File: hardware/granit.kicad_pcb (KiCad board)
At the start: 4 copper layers, 92 x 100 mm, 118 parts, among them IC1 ASM1061, J1 12V Barrel, J2 12V Screw Terminal, J3 RJ45_RB1-125B8G1A, J6 PCM12SMTR, J7 USB_C_Receptacle_USB2.0_14P, J8 BM03B-SRSS-TB, J9 SATA_22pin, Q1 FDS4435BZ, Q2 FDS4435BZ, Q3 FDS4435BZ, Q4 2N7002, Q5 2N7002, Q6 2N7002, SW1 SW_Push, U1 NCP1117-3.3_SOT223, U2 AP64501SP-13, U3 74AHCT1G125, U4 DS3231MZ, U5 USBLC6-2SC6, U6 74AHCT1G32, Y1 25MHz

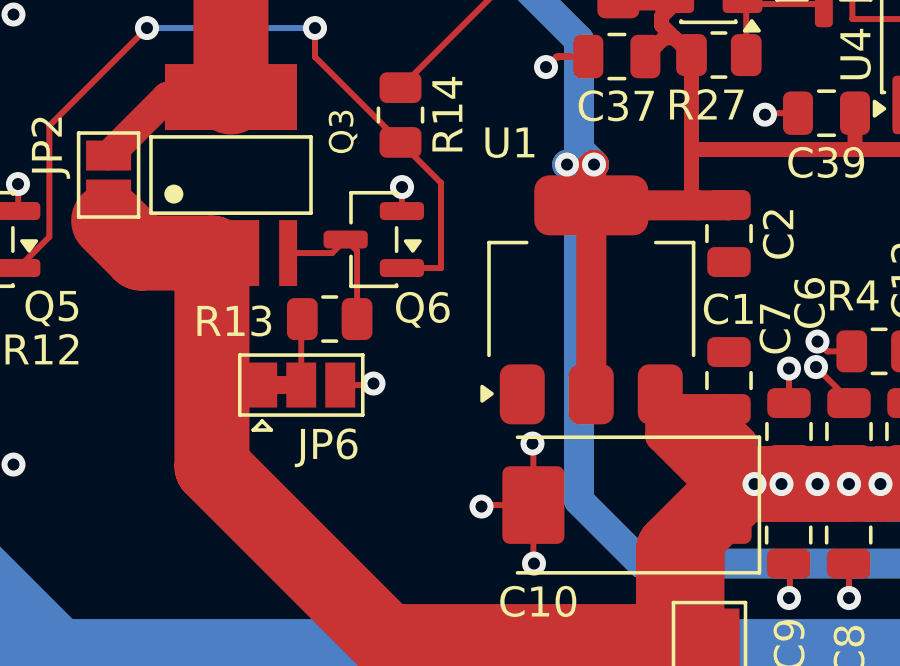
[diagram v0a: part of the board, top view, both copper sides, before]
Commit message: feat: add R15 (100K) pull-down on SATA N-FET gate for boot safety
Ensures SATA power stays OFF during boot before GPIO5 is configured.
R15 pulls Net-(Q5-G) to GND. Normal operation unaffected (3.0V at gate
with GPIO5 high, well above 2N7002 threshold).
DRC: 0 errors, 1 cosmetic warning (Y1 silkscreen).
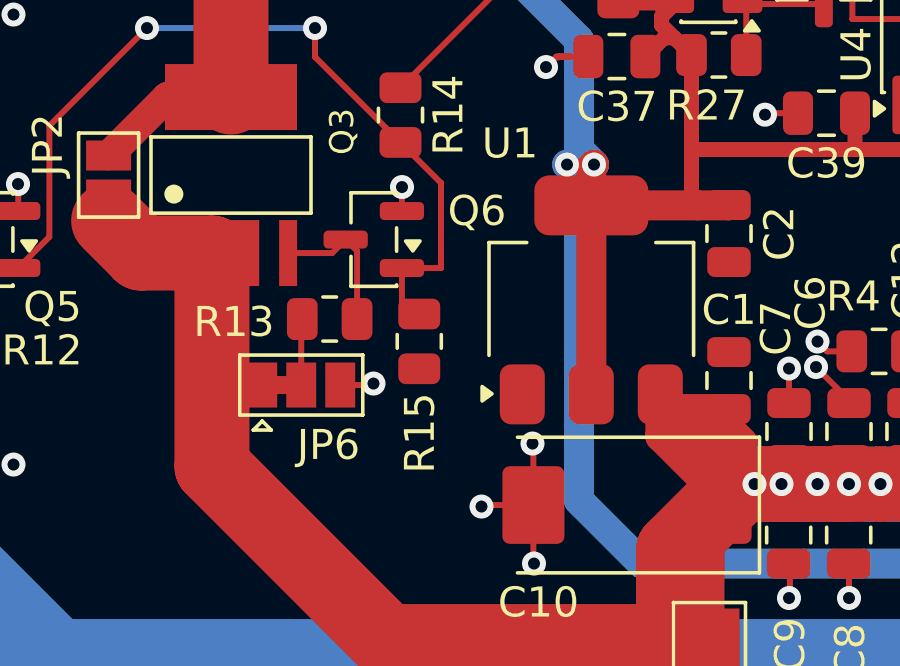
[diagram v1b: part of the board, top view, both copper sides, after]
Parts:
- added R15: 100K, Resistor_SMD:R_0805_2012Metric, F.Cu at (50.0, 107.3)
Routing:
- net Net-(Q5-G): track 26.4 -> 28.3 mm
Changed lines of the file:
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@@
 		(tags "SOT TO_SOT_SMD")
 		(property "Reference" "Q6"
-			(at -1.639999 -2.3 0)
+			(at -3.439999 0.95 0)
 			(layer "F.SilkS")
 			(effects
@@
 		)
 	)
+	(footprint "Resistor_SMD:R_0805_2012Metric"
+		(layer "F.Cu")
+		(at 49.975 107.345 90)
+		(descr "Resistor SMD 0805 (2012 Metric), square (rectangular) end terminal, IPC-7351 nominal, (Body size source: IPC-SM-782 page 72, https://www.pcb-3d.com/wordpress/wp-content/uploads/ipc-sm-782a_amendment_1_and_2.pdf)")
+		(tags "resistor")
+		(property "Reference" "R15"
+			(at -3.055 0.025 90)
+			(layer "F.SilkS")
+			(effects
+				(font
+					(size 1 1)
+					(thickness 0.15)
+				)
+			)
+		)
+		(property "Value" "100K"
+			(at 0 1.65 90)
+			(layer "F.Fab")
+			(effects
+				(font
+					(size 1 1)
+					(thickness 0.15)
+				)
+			)
+		)
+		(property "Datasheet" ""
+			(at 0 0 90)
+			(layer "F.Fab")
+			(hide yes)
+			(effects
+				(font
+					(size 1.27 1.27)
+				)
+			)
+		)
+		(property "Description" "Resistor, small symbol"
+			(at 0 0 90)
+			(layer "F.Fab")
+			(hide yes)
+			(effects
+				(font
+					(size 1.27 1.27)
+				)
+			)
+		)
+		(property "KiLib_Generator" "SMD_2terminal_chip_molded"
+			(at 0 0 90)
+			(layer "F.SilkS")
+			(hide yes)
+			(effects
+				(font
+					(size 1 1)
+					(thickness 0.15)
+				)
+			)
+		)
+		(property ki_fp_filters "R_*")
+		(sheetname "/SATA Bridge/")
+		(sheetfile "sata.kicad_sch")
+		(units
+			(unit
+				(name "A")
+				(pins "1" "2")
+			)
+		)
+		(attr smd)
+		(duplicate_pad_numbers_are_jumpers no)
+		(fp_line
+			(start -0.227064 -0.735)
+			(end 0.227064 -0.735)
+			(stroke
+				(width 0.12)
+				(type solid)
+			)
+			(layer "F.SilkS")
+		)
+		(fp_line
+			(start -0.227064 0.735)
+			(end 0.227064 0.735)
+			(stroke
+				(width 0.12)
+				(type solid)
+			)
+			(layer "F.SilkS")
+		)
+		(fp_poly
+			(pts
+				(xy -1.68 -0.95) (xy 1.68 -0.95) (xy 1.68 0.95) (xy -1.68 0.95)
+			)
+			(stroke
+				(width 0.05)
+				(type solid)
+			)
+			(fill no)
+			(layer "F.CrtYd")
+		)
+		(fp_poly
+			(pts
+				(xy -1 -0.625) (xy 1 -0.625) (xy 1 0.625) (xy -1 0.625)
+			)
+			(stroke
+				(width 0.1)
+				(type solid)
+			)
+			(fill no)
+			(layer "F.Fab")
+		)
+		(fp_text user "${REFERENCE}"
+			(at 0 0 90)
+			(layer "F.Fab")
+			(effects
+				(font
+					(size 0.5 0.5)
+					(thickness 0.08)
+				)
+			)
+		)
+		(pad "1" smd roundrect
+			(at -0.9125 0 90)
+			(size 1.025 1.4)
+			(layers "F.Cu" "F.Mask" "F.Paste")
+			(roundrect_rratio 0.243902)
+			(net "GND")
+			(pintype "passive")
+		)
+		(pad "2" smd roundrect
+			(at 0.9125 0 90)
+			(size 1.025 1.4)
+			(layers "F.Cu" "F.Mask" "F.Paste")
+			(roundrect_rratio 0.243902)
+			(net "Net-(Q5-G)")
+			(pintype "passive")
+		)
+		(embedded_fonts no)
+		(model "${KICAD10_3DMODEL_DIR}/Resistor_SMD.3dshapes/R_0805_2012Metric.step"
+			(offset
+				(xyz 0 0 0)
+			)
+			(scale
+				(xyz 1 1 1)
+			)
+			(rotate
+				(xyz 0 0 0)
+			)
+		)
+	)
 	(footprint "MountingHole:MountingHole_3.2mm_M3_Pad_Via"
 		(locked yes)
@@
 	)
 	(segment
+		(start 49.397501 104.9)
+		(end 49.397501 106.305001)
+		(width 0.2)
+		(layer "F.Cu")
+		(net "Net-(Q5-G)")
+	)
+	(segment
 		(start 50.7 102.0625)
 		(end 50.7 104.9)
@@
 		(width 0.2)
 		(layer "F.Cu")
+		(net "Net-(Q5-G)")
+	)
+	(segment
+		(start 49.397501 106.305001)
+		(end 49.725 106.6325)
+		(width 0.2)
+		(layer "F.Cu")

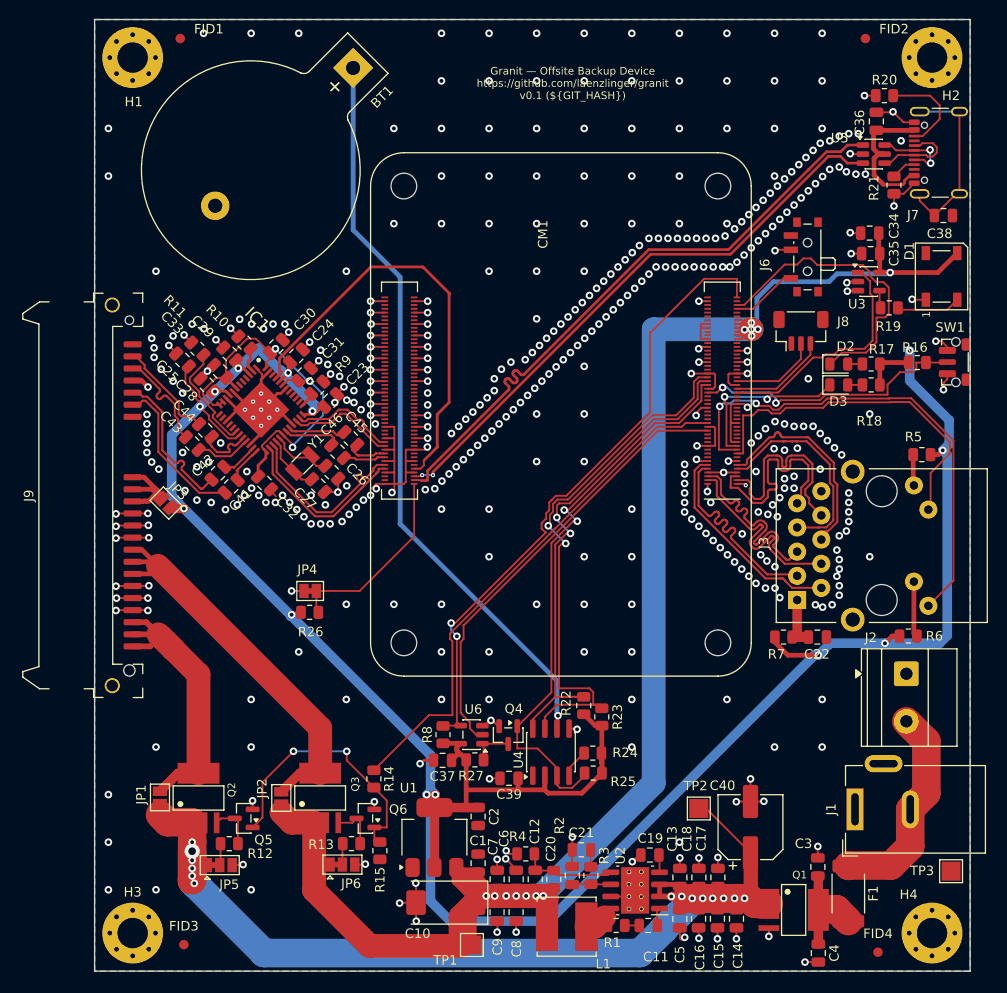
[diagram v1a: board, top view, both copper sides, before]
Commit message: feat: add silkscreen labels (knockout style)
Front: RUN/BOOT, GND TX RX, 12V, jumper functions, SATA 12V/5V, OTG
Back: stackup info (JLC04161H-7628, 4L, 100Ω diff)
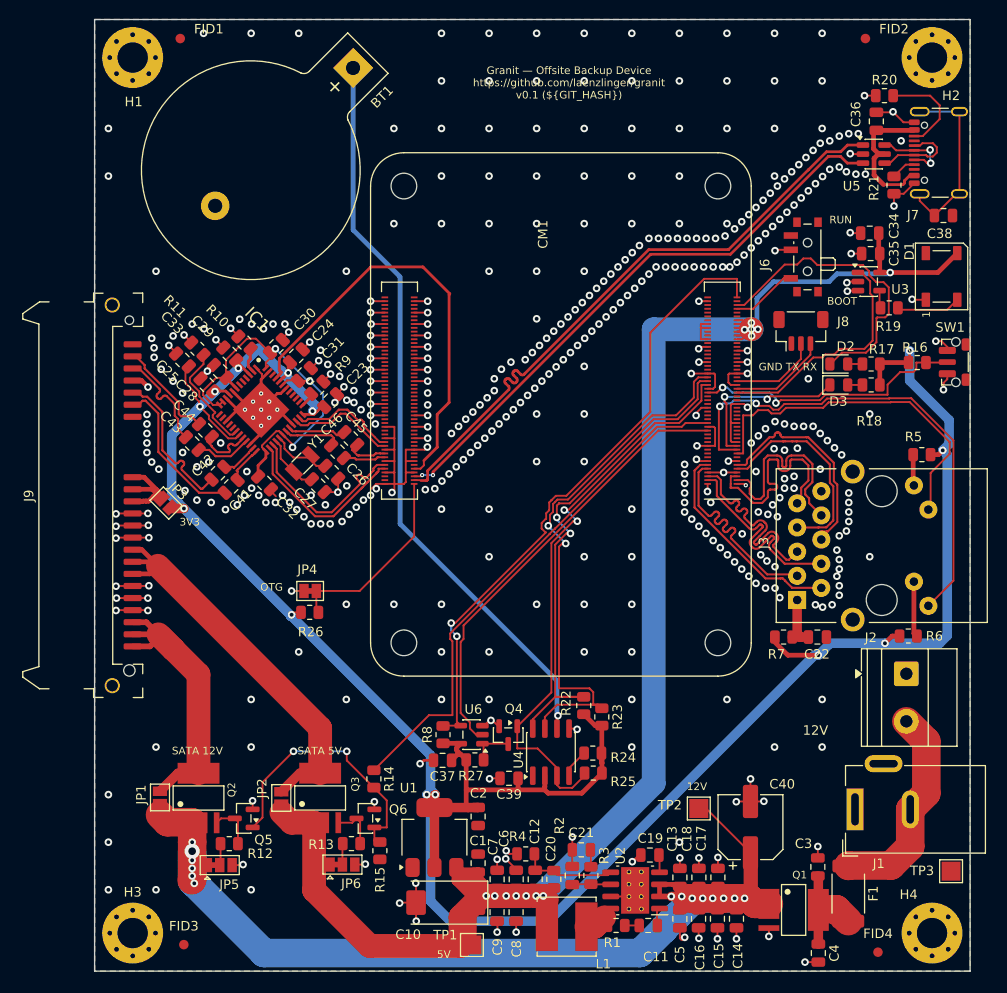
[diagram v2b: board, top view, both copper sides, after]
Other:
- board text added: "12V"
- board text added: "3V3"
- board text added: "5V"
- board text added: "BOOT"
- board text added: "GND TX RX"
- board text added: "JLC04161H-7628 | 4L 1.6mm | 100R diff"
- board text added: "OTG"
- board text added: "RUN"
- board text added: "SATA 12V"
- board text added: "SATA 5V"
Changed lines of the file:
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@@
 		(tags "capacitor electrolytic")
 		(property "Reference" "C40"
-			(at 4.37 -2.94 180)
+			(at 4.52 3.33 180)
 			(layer "F.SilkS")
 			(effects
@@
 		(tags "test point SMD pad rectangle square")
 		(property "Reference" "TP1"
-			(at -1.600001 -2.8 180)
+			(at 1.049999 -2.8 180)
 			(layer "F.SilkS")
 			(effects
@@
 		(tags "capacitor")
 		(property "Reference" "C36"
-			(at -0.1322 -1.7446 90)
+			(at 0.75 -2.15 90)
 			(layer "F.SilkS")
 			(effects
@@
 		(tags "capacitor")
 		(property "Reference" "C2"
-			(at 0 -1.679999 90)
+			(at -2.45 -0.05 180)
 			(layer "F.SilkS")
 			(effects
@@
 		(tags "SOT TO_SOT_SMD")
 		(property "Reference" "U3"
-			(at -1.25 2.3625 0)
+			(at 3.3 0.8125 0)
 			(layer "F.SilkS")
 			(effects
@@
 		(tags "test point SMD pad rectangle square")
 		(property "Reference" "TP2"
-			(at -0.35 -2.38 0)
+			(at -3.04 -0.36 0)
 			(layer "F.SilkS")
 			(effects
@@
 		(tags "connector barrel jack")
 		(property "Reference" "J1"
-			(at 0 -2.5 90)
+			(at -5.7 2.490937 180)
 			(layer "F.SilkS")
 			(effects
@@
 		(tags "capacitor tantalum")
 		(property "Reference" "C10"
-			(at 2.95 -3.250001 0)
+			(at 3.95 -3.350001 0)
 			(layer "F.SilkS")
 			(effects
@@
 		(tags "SOT TO_SOT_SMD")
 		(property "Reference" "U5"
-			(at -3.5794 -1.6915 0)
+			(at -2.3294 3.3585 0)
 			(layer "F.SilkS")
 			(effects
@@
 		(tags "resistor")
 		(property "Reference" "R24"
-			(at 3.35 -2.15 0)
+			(at 3.149999 -1.637498 0)
 			(layer "F.SilkS")
 			(effects
@@
 	)
 	(gr_text "${TITLE}\n${COMPANY}\nv${REVISION} (${GIT_HASH})"
-		(at 70.24 28.46 0)
+		(at 69.85 28.4 0)
 		(layer "F.SilkS")
 		(effects
@@
 		)
 	)
+	(gr_text "3V3"
+		(at 30 72.8 0)
+		(layer "F.SilkS" knockout)
+		(effects
+			(font
+				(size 0.8 0.8)
+				(thickness 0.15)
+			)
+		)
+	)
+	(gr_text "SATA 12V"
+		(at 30.8 96.85 0)
+		(layer "F.SilkS" knockout)
+		(effects
+			(font
+				(size 0.8 0.8)
+				(thickness 0.15)
+			)
+		)
+	)
+	(gr_text "OTG"
+		(at 38.6 79.65 0)
+		(layer "F.SilkS" knockout)
+		(effects
+			(font
+				(size 0.8 0.8)
+				(thickness 0.15)
+			)
+		)
+	)
+	(gr_text "SATA 5V"
+		(at 43.65 96.85 0)
+		(layer "F.SilkS" knockout)
+		(effects
+			(font
+				(size 0.8 0.8)
+				(thickness 0.15)
+			)
+		)
+	)
+	(gr_text "5V"
+		(at 56.7 118.25 0)
+		(layer "F.SilkS" knockout)
+		(effects
+			(font
+				(size 0.8 0.8)
+				(thickness 0.15)
+			)
+		)
+	)
+	(gr_text "12V"
+		(at 83.3 100.6 0)
+		(layer "F.SilkS" knockout)
+		(effects
+			(font
+				(size 0.8 0.8)
+				(thickness 0.15)
+			)
+		)
+	)
+	(gr_text "GND TX RX"
+		(at 92.85 56.5 0)
+		(layer "F.SilkS" knockout)
+		(effects
+			(font
+				(size 0.8 0.8)
+				(thickness 0.15)
+			)
+		)
+	)
+	(gr_text "RUN"
+		(at 98.4 41.05 0)
+		(layer "F.SilkS" knockout)
+		(effects
+			(font
+				(size 0.8 0.8)
+				(thickness 0.15)
+			)
+		)
+	)
+	(gr_text "BOOT"
+		(at 98.55 49.6 0)
+		(layer "F.SilkS" knockout)
+		(effects
+			(font
+				(size 0.8 0.8)
+				(thickness 0.15)
+			)
+		)
+	)
+	(gr_text "12V"
+		(at 95.75 94.7 0)
+		(layer "F.SilkS" knockout)
+		(effects
+			(font
+				(size 1 1)
+				(thickness 0.15)
+			)
+		)
+	)
+	(gr_text "JLC04161H-7628 | 4L 1.6mm | 100R diff"
+		(at 29.75 88.8 270)
+		(layer "B.SilkS" knockout)
+		(effects
+			(font
+				(size 0.8 0.8)
+				(thickness 0.15)
+			)
+		)
+	)

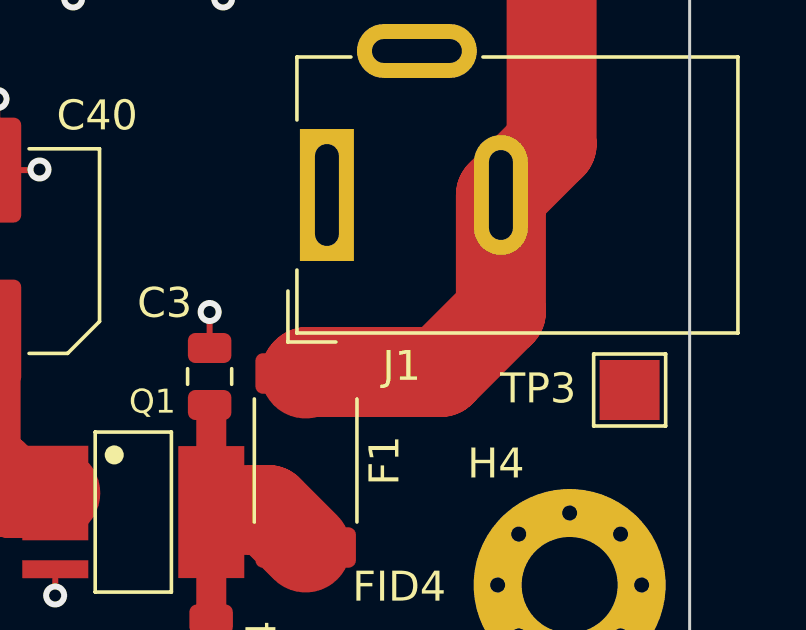
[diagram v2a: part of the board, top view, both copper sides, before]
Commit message: feat: add center-negative polarity label near J1 barrel jack
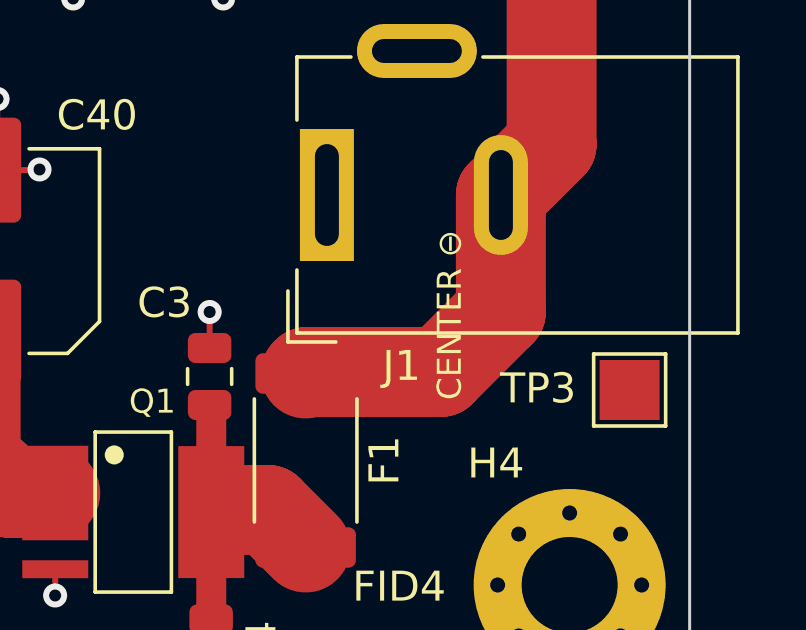
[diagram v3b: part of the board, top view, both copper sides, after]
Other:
- board text added: "CENTER ⊖"
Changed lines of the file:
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@@
+		)
+	)
+	(gr_text "CENTER ⊖"
+		(at 104 107 90)
+		(layer "F.SilkS" knockout)
+		(effects
+			(font
+				(size 0.8 0.8)
+				(thickness 0.15)
+			)
 		)
 	)

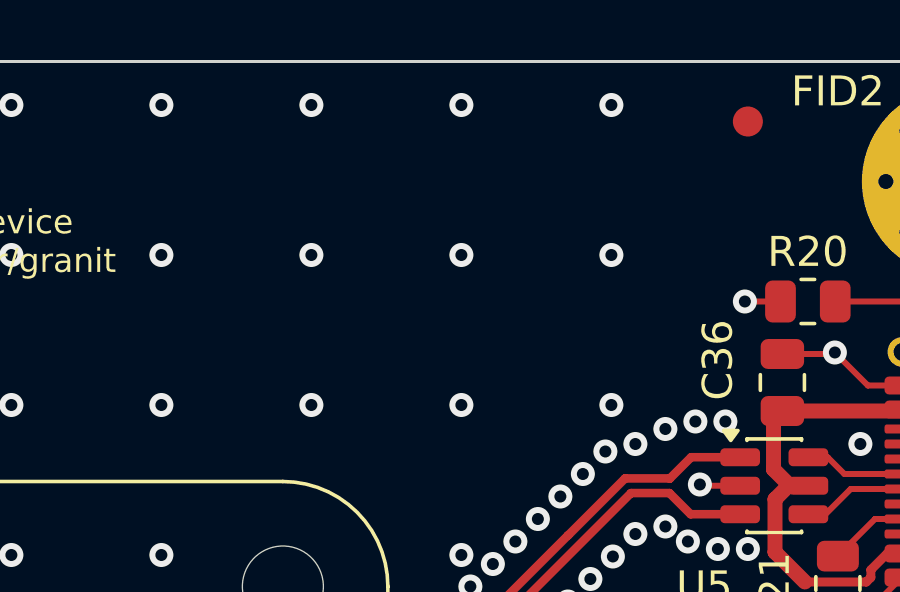
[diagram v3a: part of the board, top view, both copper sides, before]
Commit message: feat: add OSHW logo (SYM1) to schematic and PCB
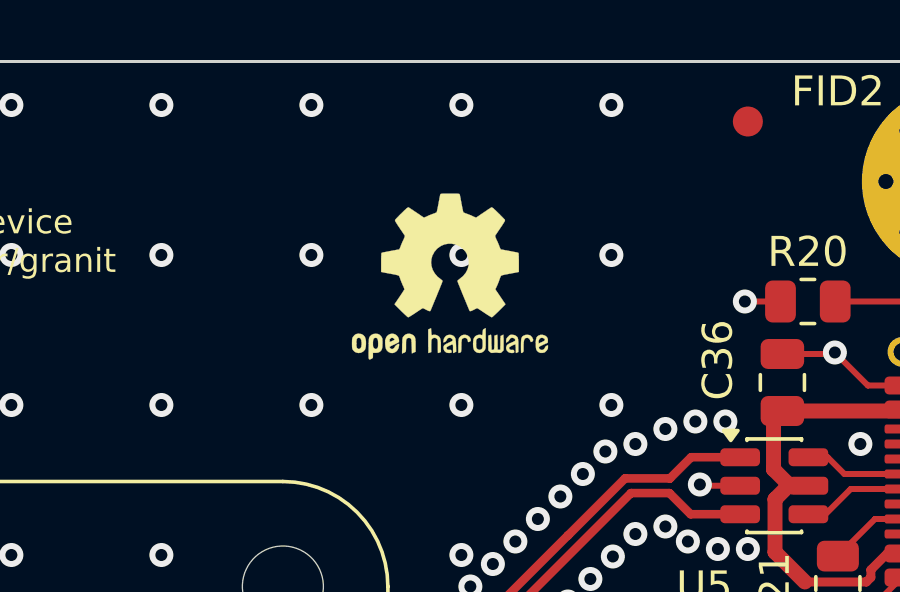
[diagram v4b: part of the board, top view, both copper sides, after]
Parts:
- added SYM1: Logo_Open_Hardware_Large, Symbol:OSHW-Logo2_7.3x6mm_SilkScreen, F.Cu at (91.1, 27.2)

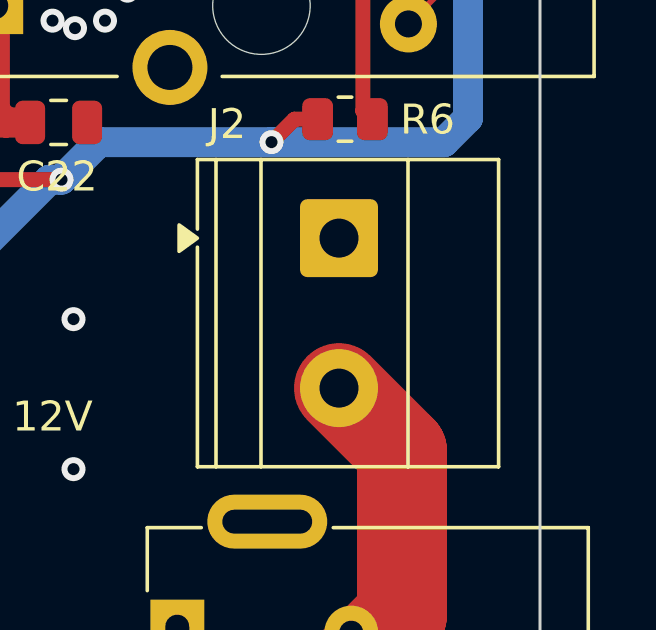
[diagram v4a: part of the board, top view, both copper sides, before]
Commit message: feat: add GND/12V knockout labels near J2 screw terminal
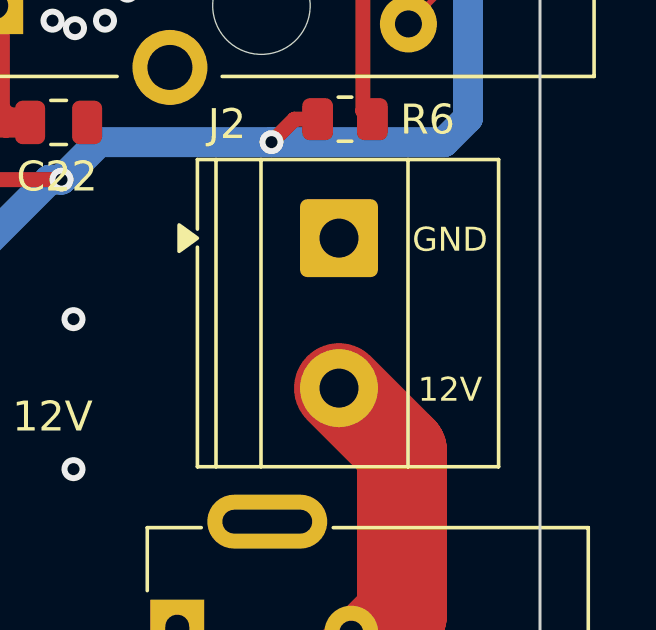
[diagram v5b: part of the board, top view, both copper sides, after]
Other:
- board text added: "GND"
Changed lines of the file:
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@@
+		)
+	)
+	(gr_text "GND"
+		(at 109 88.8 0)
+		(layer "F.SilkS" knockout)
+		(effects
+			(font
+				(size 0.8 0.8)
+				(thickness 0.15)
+			)
+		)
+	)
+	(gr_text "12V"
+		(at 109 93.8 0)
+		(layer "F.SilkS" knockout)
+		(effects
+			(font
+				(size 0.8 0.8)
+				(thickness 0.15)
+			)
 		)
 	)
